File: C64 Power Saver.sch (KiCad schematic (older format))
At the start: 15 parts, among them J1 INPUT, J2 OUTPUT, K1 SANYOU_SRD_Form_C, Q1 PN2222A, Q2 PN2222A

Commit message: Added screw terminals for 9VAC
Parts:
- added J3: 9VAC_INPUT, symbol Screw_Terminal_01x02
- added J4: 9VAC_OUTPUT, symbol Screw_Terminal_01x02
- J1: value INPUT -> 5V_INPUT
- J2: value OUTPUT -> 5V_OUTPUT; symbol POWER -> OUTPUT
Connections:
- wire segments 36 -> 38
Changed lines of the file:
@@
 P 10400 825
 F 0 "J1" H 10400 925 50  0000 C CNN
-F 1 "INPUT" H 10400 625 50  0000 C CNN
+F 1 "5V_INPUT" H 10400 625 50  0000 C CNN
 F 2 "" H 10400 825 50  0001 C CNN
 F 3 "" H 10400 825 50  0001 C CNN
@@
 $EndComp
 $Comp
-L POWER J2
+L OUTPUT J2
 U 1 1 5B8BE0D9
 P 10400 1400
 F 0 "J2" H 10400 1500 50  0000 C CNN
-F 1 "OUTPUT" H 10400 1200 50  0000 C CNN
+F 1 "5V_OUTPUT" H 10400 1200 50  0000 C CNN
 F 2 "" H 10400 1400 50  0001 C CNN
 F 3 "" H 10400 1400 50  0001 C CNN
@@
 	9925 925  9925 1625
 Connection ~ 9925 1500
+$Comp
+L Screw_Terminal_01x02 J3
+U 1 1 5B8C3D4A
+P 8250 925
+F 0 "J3" H 8250 1025 50  0000 C CNN
+F 1 "9VAC_INPUT" H 8250 725 50  0000 C CNN
+F 2 "" H 8250 925 50  0001 C CNN
+F 3 "" H 8250 925 50  0001 C CNN
+	1    8250 925
+	-1   0    0    1
+$EndComp
+$Comp
+L Screw_Terminal_01x02 J4
+U 1 1 5B8C3DC4
+P 9125 825
+F 0 "J4" H 9125 925 50  0000 C CNN
+F 1 "9VAC_OUTPUT" H 9125 625 50  0000 C CNN
+F 2 "" H 9125 825 50  0001 C CNN
+F 3 "" H 9125 825 50  0001 C CNN
+	1    9125 825
+	1    0    0    -1
+$EndComp
+Wire Wire Line
+	8925 825  8450 825
+Wire Wire Line
+	8450 925  8925 925
 $EndSCHEMATC

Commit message: PCB layout done
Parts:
- D1, D2: footprint (none) -> Diodes_THT:D_DO-35_SOD27_P10.16mm_Horizontal
- D3: value LED -> OK; footprint (none) -> LEDs:LED_D5.0mm
- D4: value LED -> OV; footprint (none) -> LEDs:LED_D5.0mm
- F1: footprint (none) -> Fuse_Holders_and_Fuses:Fuseholder5x20_horiz_SemiClosed_Casing10x25mm
- J1, J2, J3, J4: footprint (none) -> Connectors_Terminal_Blocks:TerminalBlock_bornier-2_P5.08mm
- R1, R2, R3, R4, R5: footprint (none) -> Resistors_THT:R_Axial_DIN0207_L6.3mm_D2.5mm_P10.16mm_Horizontal
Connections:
- net labels added: 5V_IN, 5V_OUT, 9VAC_1, 9VAC_2
- net labels removed: VDD
- wire segments 38 -> 40
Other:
- moved on the sheet: J2, J4
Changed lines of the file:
@@
 F 0 "R1" V 2480 2075 50  0000 C CNN
 F 1 "470" V 2400 2075 50  0000 C CNN
-F 2 "" V 2330 2075 50  0001 C CNN
+F 2 "Resistors_THT:R_Axial_DIN0207_L6.3mm_D2.5mm_P10.16mm_Horizontal" V 2330 2075 50  0001 C CNN
 F 3 "" H 2400 2075 50  0001 C CNN
 	1    2400 2075
@@
 F 0 "R2" V 2480 3400 50  0000 C CNN
 F 1 "470" V 2400 3400 50  0000 C CNN
-F 2 "" V 2330 3400 50  0001 C CNN
+F 2 "Resistors_THT:R_Axial_DIN0207_L6.3mm_D2.5mm_P10.16mm_Horizontal" V 2330 3400 50  0001 C CNN
 F 3 "" H 2400 3400 50  0001 C CNN
 	1    2400 3400
@@
 F 0 "R3" V 2955 2075 50  0000 C CNN
 F 1 "2k2" V 2875 2075 50  0000 C CNN
-F 2 "" V 2805 2075 50  0001 C CNN
+F 2 "Resistors_THT:R_Axial_DIN0207_L6.3mm_D2.5mm_P10.16mm_Horizontal" V 2805 2075 50  0001 C CNN
 F 3 "" H 2875 2075 50  0001 C CNN
 	1    2875 2075
@@
 F 0 "D1" H 2400 2750 50  0000 C CNN
 F 1 "4.7v" H 2400 2550 50  0000 C CNN
-F 2 "" H 2400 2650 50  0001 C CNN
+F 2 "Diodes_THT:D_DO-35_SOD27_P10.16mm_Horizontal" H 2400 2650 50  0001 C CNN
 F 3 "" H 2400 2650 50  0001 C CNN
 	1    2400 2650
@@
 F 0 "D2" H 3425 2175 50  0000 C CNN
 F 1 "1N914" H 3425 1975 50  0000 C CNN
-F 2 "" H 3425 2075 50  0001 C CNN
+F 2 "Diodes_THT:D_DO-35_SOD27_P10.16mm_Horizontal" H 3425 2075 50  0001 C CNN
 F 3 "" H 3425 2075 50  0001 C CNN
 	1    3425 2075
@@
 F 0 "R5" V 5630 3525 50  0000 C CNN
 F 1 "470" V 5550 3525 50  0000 C CNN
-F 2 "" V 5480 3525 50  0001 C CNN
+F 2 "Resistors_THT:R_Axial_DIN0207_L6.3mm_D2.5mm_P10.16mm_Horizontal" V 5480 3525 50  0001 C CNN
 F 3 "" H 5550 3525 50  0001 C CNN
 	1    5550 3525
@@
 F 0 "R4" V 5280 3525 50  0000 C CNN
 F 1 "470" V 5200 3525 50  0000 C CNN
-F 2 "" V 5130 3525 50  0001 C CNN
+F 2 "Resistors_THT:R_Axial_DIN0207_L6.3mm_D2.5mm_P10.16mm_Horizontal" V 5130 3525 50  0001 C CNN
 F 3 "" H 5200 3525 50  0001 C CNN
 	1    5200 3525
@@
 P 5550 3975
 F 0 "D4" H 5550 4075 50  0000 C CNN
-F 1 "LED" H 5550 3875 50  0000 C CNN
-F 2 "" H 5550 3975 50  0001 C CNN
+F 1 "OV" H 5550 3875 50  0000 C CNN
+F 2 "LEDs:LED_D5.0mm" H 5550 3975 50  0001 C CNN
 F 3 "" H 5550 3975 50  0001 C CNN
 	1    5550 3975
@@
 P 5200 3975
 F 0 "D3" H 5200 4075 50  0000 C CNN
-F 1 "LED" H 5200 3875 50  0000 C CNN
-F 2 "" H 5200 3975 50  0001 C CNN
+F 1 "OK" H 5200 3875 50  0000 C CNN
+F 2 "LEDs:LED_D5.0mm" H 5200 3975 50  0001 C CNN
 F 3 "" H 5200 3975 50  0001 C CNN
 	1    5200 3975
@@
 F 0 "F1" V 1980 1800 50  0000 C CNN
 F 1 "1.5A" V 1825 1800 50  0000 C CNN
-F 2 "" V 1830 1800 50  0001 C CNN
+F 2 "Fuse_Holders_and_Fuses:Fuseholder5x20_horiz_SemiClosed_Casing10x25mm" V 1830 1800 50  0001 C CNN
 F 3 "" H 1900 1800 50  0001 C CNN
 	1    1900 1800
 	0    1    1    0
 $EndComp
-$Comp
-L VCC #PWR02
-U 1 1 5B8BD26B
-P 1625 1675
-F 0 "#PWR02" H 1625 1525 50  0001 C CNN
-F 1 "VCC" H 1625 1825 50  0000 C CNN
-F 2 "" H 1625 1675 50  0001 C CNN
-F 3 "" H 1625 1675 50  0001 C CNN
-	1    1625 1675
-	1    0    0    -1
-$EndComp
 Wire Wire Line
 	2400 2800 2400 3250
@@
 Connection ~ 5200 2850
 $Comp
-L VCC #PWR03
+L VCC #PWR02
 U 1 1 5B8BE9DD
 P 10075 700
-F 0 "#PWR03" H 10075 550 50  0001 C CNN
+F 0 "#PWR02" H 10075 550 50  0001 C CNN
 F 1 "VCC" H 10075 850 50  0000 C CNN
 F 2 "" H 10075 700 50  0001 C CNN
@@
 $EndComp
 Wire Wire Line
-	10075 1275 10075 1400
-Wire Wire Line
-	10075 1400 10200 1400
-Wire Wire Line
 	10075 700  10075 825
 Wire Wire Line
-	10075 825  10200 825
-$Comp
-L VDD #PWR04
-U 1 1 5B8BF5F3
-P 5200 1675
-F 0 "#PWR04" H 5200 1525 50  0001 C CNN
-F 1 "VDD" H 5200 1825 50  0000 C CNN
-F 2 "" H 5200 1675 50  0001 C CNN
-F 3 "" H 5200 1675 50  0001 C CNN
-	1    5200 1675
-	1    0    0    -1
-$EndComp
-$Comp
-L VDD #PWR05
-U 1 1 5B8BF704
-P 10075 1275
-F 0 "#PWR05" H 10075 1125 50  0001 C CNN
-F 1 "VDD" H 10075 1425 50  0000 C CNN
-F 2 "" H 10075 1275 50  0001 C CNN
-F 3 "" H 10075 1275 50  0001 C CNN
-	1    10075 1275
-	1    0    0    -1
-$EndComp
+	9950 825  10200 825
 $Comp
 L POWER J1
@@
 F 0 "J1" H 10400 925 50  0000 C CNN
 F 1 "5V_INPUT" H 10400 625 50  0000 C CNN
-F 2 "" H 10400 825 50  0001 C CNN
+F 2 "Connectors_Terminal_Blocks:TerminalBlock_bornier-2_P5.08mm" H 10400 825 50  0001 C CNN
 F 3 "" H 10400 825 50  0001 C CNN
 	1    10400 825
@@
 L OUTPUT J2
 U 1 1 5B8BE0D9
-P 10400 1400
-F 0 "J2" H 10400 1500 50  0000 C CNN
-F 1 "5V_OUTPUT" H 10400 1200 50  0000 C CNN
-F 2 "" H 10400 1400 50  0001 C CNN
-F 3 "" H 10400 1400 50  0001 C CNN
-	1    10400 1400
-	1    0    0    -1
-$EndComp
-Wire Wire Line
-	9925 1500 10200 1500
-Wire Wire Line
-	9925 925  10200 925
-$Comp
-L GND #PWR06
+P 10400 1250
+F 0 "J2" H 10400 1350 50  0000 C CNN
+F 1 "5V_OUTPUT" H 10400 1050 50  0000 C CNN
+F 2 "Connectors_Terminal_Blocks:TerminalBlock_bornier-2_P5.08mm" H 10400 1250 50  0001 C CNN
+F 3 "" H 10400 1250 50  0001 C CNN
+	1    10400 1250
+	1    0    0    -1
+$EndComp
+$Comp
+L GND #PWR03
 U 1 1 5B8C250E
-P 9925 1625
-F 0 "#PWR06" H 9925 1375 50  0001 C CNN
-F 1 "GND" H 9925 1475 50  0000 C CNN
-F 2 "" H 9925 1625 50  0001 C CNN
-F 3 "" H 9925 1625 50  0001 C CNN
-	1    9925 1625
-	1    0    0    -1
-$EndComp
-Wire Wire Line
-	9925 925  9925 1625
-Connection ~ 9925 1500
+P 9900 1350
+F 0 "#PWR03" H 9900 1100 50  0001 C CNN
+F 1 "GND" H 9900 1200 50  0000 C CNN
+F 2 "" H 9900 1350 50  0001 C CNN
+F 3 "" H 9900 1350 50  0001 C CNN
+	1    9900 1350
+	1    0    0    -1
+$EndComp
 $Comp
 L Screw_Terminal_01x02 J3
@@
 F 0 "J3" H 8250 1025 50  0000 C CNN
 F 1 "9VAC_INPUT" H 8250 725 50  0000 C CNN
-F 2 "" H 8250 925 50  0001 C CNN
+F 2 "Connectors_Terminal_Blocks:TerminalBlock_bornier-2_P5.08mm" H 8250 925 50  0001 C CNN
 F 3 "" H 8250 925 50  0001 C CNN
 	1    8250 925
@@
 L Screw_Terminal_01x02 J4
 U 1 1 5B8C3DC4
-P 9125 825
-F 0 "J4" H 9125 925 50  0000 C CNN
-F 1 "9VAC_OUTPUT" H 9125 625 50  0000 C CNN
-F 2 "" H 9125 825 50  0001 C CNN
-F 3 "" H 9125 825 50  0001 C CNN
-	1    9125 825
-	1    0    0    -1
-$EndComp
-Wire Wire Line
-	8925 825  8450 825
-Wire Wire Line
-	8450 925  8925 925
+P 8250 1425
+F 0 "J4" H 8250 1525 50  0000 C CNN
+F 1 "9VAC_OUTPUT" H 8250 1225 50  0000 C CNN
+F 2 "Connectors_Terminal_Blocks:TerminalBlock_bornier-2_P5.08mm" H 8250 1425 50  0001 C CNN
+F 3 "" H 8250 1425 50  0001 C CNN
+	1    8250 1425
+	-1   0    0    1
+$EndComp
+Text GLabel 5200 1675 1    60   Output ~ 0
+5V_OUT
+Text GLabel 1625 1675 1    60   Input ~ 0
+5V_IN
+Text GLabel 9950 825  0    60   Output ~ 0
+5V_IN
+Connection ~ 10075 825
+Text GLabel 10075 1475 3    60   Input ~ 0
+5V_OUT
+Wire Wire Line
+	10075 1475 10075 1350
+Wire Wire Line
+	10075 1350 10200 1350
+Wire Wire Line
+	9900 1350 9900 925
+Wire Wire Line
+	9900 925  10200 925
+Wire Wire Line
+	10200 1250 9900 1250
+Connection ~ 9900 1250
+Text GLabel 8575 825  2    60   BiDi ~ 0
+9VAC_1
+Wire Wire Line
+	8450 825  8575 825
+Text GLabel 8575 1425 2    60   BiDi ~ 0
+9VAC_1
+Wire Wire Line
+	8450 1325 8575 1325
+Text GLabel 8575 925  2    60   BiDi ~ 0
+9VAC_2
+Text GLabel 8575 1325 2    60   BiDi ~ 0
+9VAC_2
+Wire Wire Line
+	8450 1425 8575 1425
+Wire Wire Line
+	8450 925  8575 925
 $EndSCHEMATC

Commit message: DIN connector sketch (pads need measuring)
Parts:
- added J5: DIN-7, symbol DIN-7
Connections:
- net 9VAC_1: now also J5.7
- net 9VAC_2: now also J5.6
- net GND: now also J5.2
- net VCC: now also J5.5
- no-connect marks 0 -> 3
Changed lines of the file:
@@
 Wire Wire Line
 	8450 925  8575 925
+$Comp
+L DIN-7 J5
+U 1 1 5B8CBE3E
+P 10075 2650
+F 0 "J5" H 10200 2875 50  0000 C CNN
+F 1 "DIN-7" H 10075 2390 50  0000 C CNN
+F 2 "" H 10075 2650 50  0001 C CNN
+F 3 "" H 10075 2650 50  0001 C CNN
+	1    10075 2650
+	-1   0    0    1
+$EndComp
+$Comp
+L GND #PWR04
+U 1 1 5B8CC381
+P 10075 3075
+F 0 "#PWR04" H 10075 2825 50  0001 C CNN
+F 1 "GND" H 10075 2925 50  0000 C CNN
+F 2 "" H 10075 3075 50  0001 C CNN
+F 3 "" H 10075 3075 50  0001 C CNN
+	1    10075 3075
+	1    0    0    -1
+$EndComp
+Wire Wire Line
+	10075 3075 10075 2950
+NoConn ~ 10375 2650
+NoConn ~ 9775 2650
+NoConn ~ 10375 2750
+Text GLabel 9675 2750 0    60   Output ~ 0
+5V_IN
+Wire Wire Line
+	9675 2750 9775 2750
+Text GLabel 9675 2550 0    60   BiDi ~ 0
+9VAC_1
+Text GLabel 10500 2550 2    60   BiDi ~ 0
+9VAC_2
+Wire Wire Line
+	9675 2550 9775 2550
+Wire Wire Line
+	10375 2550 10500 2550
 $EndSCHEMATC

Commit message: Oh... So I made a saver that works only on bad ones... Rev. B!
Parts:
- D1: value 4.7v -> 1N4732A
- D2: value 1N914 -> 1N4148
- D4: value OV -> BAD
- Q1, Q2: footprint TO_SOT_Packages_THT:TO-92_Molded_Narrow -> TO_SOT_Packages_THT:TO-92_Inline_Wide
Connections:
- net 5V_OUT: now also K1.3; no longer K1.4
- net at R5.1: now also K1.4; no longer K1.3
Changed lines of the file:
@@
 P 2400 2650
 F 0 "D1" H 2400 2750 50  0000 C CNN
-F 1 "4.7v" H 2400 2550 50  0000 C CNN
+F 1 "1N4732A" H 2400 2550 50  0000 C CNN
 F 2 "Diodes_THT:D_DO-35_SOD27_P10.16mm_Horizontal" H 2400 2650 50  0001 C CNN
 F 3 "" H 2400 2650 50  0001 C CNN
@@
 F 0 "Q1" H 2975 3100 50  0000 L CNN
 F 1 "PN2222A" H 2975 3025 50  0000 L CNN
-F 2 "TO_SOT_Packages_THT:TO-92_Molded_Narrow" H 2975 2950 50  0001 L CIN
+F 2 "TO_SOT_Packages_THT:TO-92_Inline_Wide" H 2975 2950 50  0001 L CIN
 F 3 "" H 2775 3025 50  0001 L CNN
 	1    2775 3025
@@
 P 3425 2075
 F 0 "D2" H 3425 2175 50  0000 C CNN
-F 1 "1N914" H 3425 1975 50  0000 C CNN
+F 1 "1N4148" H 3425 1975 50  0000 C CNN
 F 2 "Diodes_THT:D_DO-35_SOD27_P10.16mm_Horizontal" H 3425 2075 50  0001 C CNN
 F 3 "" H 3425 2075 50  0001 C CNN
@@
 F 0 "Q2" H 3525 2725 50  0000 L CNN
 F 1 "PN2222A" H 3525 2650 50  0000 L CNN
-F 2 "TO_SOT_Packages_THT:TO-92_Molded_Narrow" H 3525 2575 50  0001 L CIN
+F 2 "TO_SOT_Packages_THT:TO-92_Inline_Wide" H 3525 2575 50  0001 L CIN
 F 3 "" H 3325 2650 50  0001 L CNN
 	1    3325 2650
@@
 P 5550 3975
 F 0 "D4" H 5550 4075 50  0000 C CNN
-F 1 "OV" H 5550 3875 50  0000 C CNN
+F 1 "BAD" H 5550 3875 50  0000 C CNN
 F 2 "LEDs:LED_D5.0mm" H 5550 3975 50  0001 C CNN
 F 3 "" H 5550 3975 50  0001 C CNN
@@
 	5550 4275 5550 4125
 Wire Wire Line
-	4750 2850 5200 2850
-Wire Wire Line
 	5200 1675 5200 3375
-Wire Wire Line
-	5550 2650 5550 3375
 Connection ~ 2400 1800
 Wire Wire Line
@@
 	5200 4125 5200 4275
 Connection ~ 5200 4275
-Wire Wire Line
-	4750 2650 5550 2650
-Connection ~ 5200 2850
 $Comp
 L VCC #PWR02
@@
 	10075 1350 10200 1350
 Wire Wire Line
-	9900 1350 9900 925
+	9900 925  9900 1350
 Wire Wire Line
 	9900 925  10200 925
@@
 Wire Wire Line
 	10375 2550 10500 2550
+Wire Wire Line
+	4750 2650 5200 2650
+Connection ~ 5200 2650
+Wire Wire Line
+	4750 2850 5550 2850
+Wire Wire Line
+	5550 2850 5550 3375
 $EndSCHEMATC

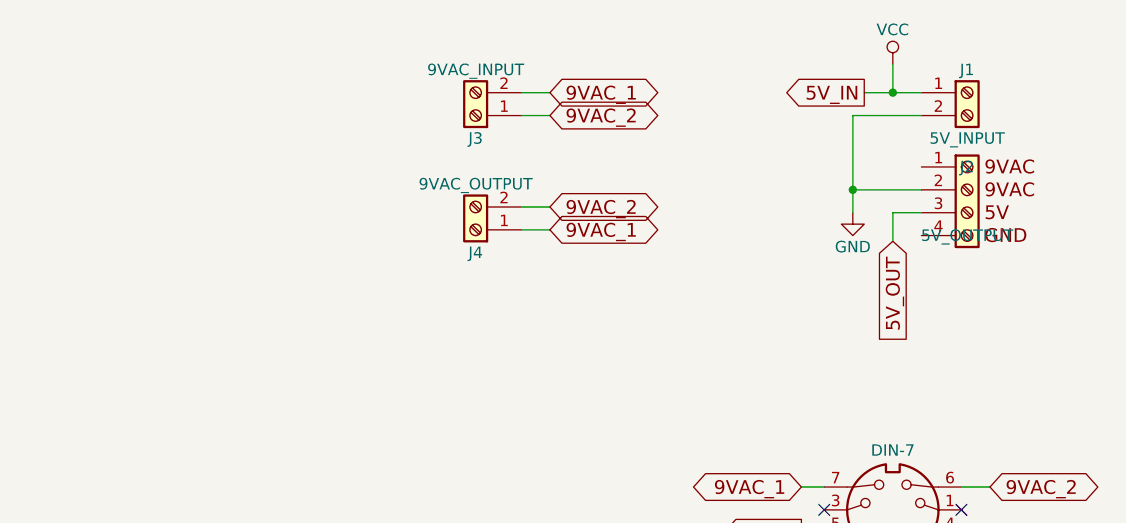
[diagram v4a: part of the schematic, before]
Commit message: Updated schematic to use DIN connector and wire points
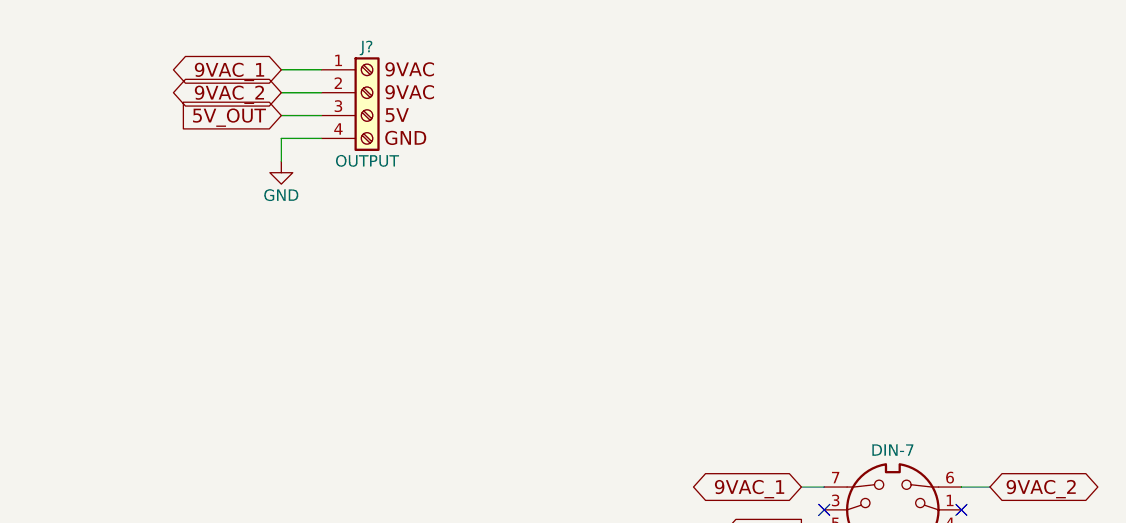
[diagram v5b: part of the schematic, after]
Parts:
- removed J1: 5V_INPUT, Connectors_Terminal_Blocks:TerminalBlock_bornier-2_P5.08mm, symbol POWER
- removed J2: 5V_OUTPUT, Connectors_Terminal_Blocks:TerminalBlock_bornier-2_P5.08mm, symbol OUTPUT
- removed J3: 9VAC_INPUT, Connectors_Terminal_Blocks:TerminalBlock_bornier-2_P5.08mm, symbol Screw_Terminal_01x02
- removed J4: 9VAC_OUTPUT, Connectors_Terminal_Blocks:TerminalBlock_bornier-2_P5.08mm, symbol Screw_Terminal_01x02
- added J?: OUTPUT, symbol OUTPUT
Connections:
- net 5V_OUT: now also J?.3 (Pin_3)
- net 9VAC_1: now also J?.1 (Pin_1)
- net 9VAC_2: now also J?.2 (Pin_2)
- net GND: now also J?.4 (Pin_4)
- net VCC renamed 5V_IN
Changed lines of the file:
@@
 	5200 4125 5200 4275
 Connection ~ 5200 4275
-$Comp
-L VCC #PWR02
-U 1 1 5B8BE9DD
-P 10075 700
-F 0 "#PWR02" H 10075 550 50  0001 C CNN
-F 1 "VCC" H 10075 850 50  0000 C CNN
-F 2 "" H 10075 700 50  0001 C CNN
-F 3 "" H 10075 700 50  0001 C CNN
-	1    10075 700
-	1    0    0    -1
-$EndComp
-Wire Wire Line
-	10075 700  10075 825
-Wire Wire Line
-	9950 825  10200 825
-$Comp
-L POWER J1
-U 1 1 5B8BFF1C
-P 10400 825
-F 0 "J1" H 10400 925 50  0000 C CNN
-F 1 "5V_INPUT" H 10400 625 50  0000 C CNN
-F 2 "Connectors_Terminal_Blocks:TerminalBlock_bornier-2_P5.08mm" H 10400 825 50  0001 C CNN
-F 3 "" H 10400 825 50  0001 C CNN
-	1    10400 825
-	1    0    0    -1
-$EndComp
-$Comp
-L OUTPUT J2
-U 1 1 5B8BE0D9
-P 10400 1250
-F 0 "J2" H 10400 1350 50  0000 C CNN
-F 1 "5V_OUTPUT" H 10400 1050 50  0000 C CNN
-F 2 "Connectors_Terminal_Blocks:TerminalBlock_bornier-2_P5.08mm" H 10400 1250 50  0001 C CNN
-F 3 "" H 10400 1250 50  0001 C CNN
-	1    10400 1250
-	1    0    0    -1
-$EndComp
-$Comp
-L GND #PWR03
-U 1 1 5B8C250E
-P 9900 1350
-F 0 "#PWR03" H 9900 1100 50  0001 C CNN
-F 1 "GND" H 9900 1200 50  0000 C CNN
-F 2 "" H 9900 1350 50  0001 C CNN
-F 3 "" H 9900 1350 50  0001 C CNN
-	1    9900 1350
-	1    0    0    -1
-$EndComp
-$Comp
-L Screw_Terminal_01x02 J3
-U 1 1 5B8C3D4A
-P 8250 925
-F 0 "J3" H 8250 1025 50  0000 C CNN
-F 1 "9VAC_INPUT" H 8250 725 50  0000 C CNN
-F 2 "Connectors_Terminal_Blocks:TerminalBlock_bornier-2_P5.08mm" H 8250 925 50  0001 C CNN
-F 3 "" H 8250 925 50  0001 C CNN
-	1    8250 925
-	-1   0    0    1
-$EndComp
-$Comp
-L Screw_Terminal_01x02 J4
-U 1 1 5B8C3DC4
-P 8250 1425
-F 0 "J4" H 8250 1525 50  0000 C CNN
-F 1 "9VAC_OUTPUT" H 8250 1225 50  0000 C CNN
-F 2 "Connectors_Terminal_Blocks:TerminalBlock_bornier-2_P5.08mm" H 8250 1425 50  0001 C CNN
-F 3 "" H 8250 1425 50  0001 C CNN
-	1    8250 1425
-	-1   0    0    1
-$EndComp
 Text GLabel 5200 1675 1    60   Output ~ 0
 5V_OUT
 Text GLabel 1625 1675 1    60   Input ~ 0
 5V_IN
-Text GLabel 9950 825  0    60   Output ~ 0
-5V_IN
-Connection ~ 10075 825
-Text GLabel 10075 1475 3    60   Input ~ 0
-5V_OUT
-Wire Wire Line
-	10075 1475 10075 1350
-Wire Wire Line
-	10075 1350 10200 1350
-Wire Wire Line
-	9900 925  9900 1350
-Wire Wire Line
-	9900 925  10200 925
-Wire Wire Line
-	10200 1250 9900 1250
-Connection ~ 9900 1250
-Text GLabel 8575 825  2    60   BiDi ~ 0
+Text GLabel 7400 725  0    60   BiDi ~ 0
 9VAC_1
-Wire Wire Line
-	8450 825  8575 825
-Text GLabel 8575 1425 2    60   BiDi ~ 0
-9VAC_1
-Wire Wire Line
-	8450 1325 8575 1325
-Text GLabel 8575 925  2    60   BiDi ~ 0
+Text GLabel 7400 825  0    60   BiDi ~ 0
 9VAC_2
-Text GLabel 8575 1325 2    60   BiDi ~ 0
-9VAC_2
-Wire Wire Line
-	8450 1425 8575 1425
-Wire Wire Line
-	8450 925  8575 925
 $Comp
 L DIN-7 J5
@@
 $EndComp
 $Comp
-L GND #PWR04
+L GND #PWR02
 U 1 1 5B8CC381
 P 10075 3075
-F 0 "#PWR04" H 10075 2825 50  0001 C CNN
+F 0 "#PWR02" H 10075 2825 50  0001 C CNN
 F 1 "GND" H 10075 2925 50  0000 C CNN
 F 2 "" H 10075 3075 50  0001 C CNN
@@
 Wire Wire Line
 	5550 2850 5550 3375
+Wire Wire Line
+	7400 725  7575 725
+Wire Wire Line
+	7400 825  7575 825
+Text GLabel 7400 925  0    60   Input ~ 0
+5V_OUT
+$Comp
+L GND #PWR03
+U 1 1 5BB0E370
+P 7400 1125
+F 0 "#PWR03" H 7400 875 50  0001 C CNN
+F 1 "GND" H 7400 975 50  0000 C CNN
+F 2 "" H 7400 1125 50  0001 C CNN
+F 3 "" H 7400 1125 50  0001 C CNN
+	1    7400 1125
+	1    0    0    -1
+$EndComp
+Wire Wire Line
+	7400 925  7575 925
+Wire Wire Line
+	7575 1025 7400 1025
+Wire Wire Line
+	7400 1025 7400 1125
+$Comp
+L OUTPUT J?
+U 1 1 5BB0E936
+P 7775 825
+F 0 "J?" H 7775 1025 50  0000 C CNN
+F 1 "OUTPUT" H 7775 525 50  0000 C CNN
+F 2 "" H 7775 825 50  0001 C CNN
+F 3 "" H 7775 825 50  0001 C CNN
+	1    7775 825
+	1    0    0    -1
+$EndComp
 $EndSCHEMATC

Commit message: PCB layout redone with DIN connector and added 5v buzzer
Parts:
- added BZ1: Buzzer, Buzzers_Beepers:Buzzer_12x9.5RM7.6, symbol Buzzer
- D1: footprint Diodes_THT:D_DO-35_SOD27_P10.16mm_Horizontal -> Diodes_THT:D_T-1_P10.16mm_Horizontal
- J1: renamed from J?; footprint (none) -> C64_PWR:OUTPUT_ZIP
- J5: footprint (none) -> C64_PWR:C64_PWR
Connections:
- net 9VAC_1: now also J1.2 (Pin_2); no longer J1.1 (Pin_1)
- net 9VAC_2: now also J1.1 (Pin_1); no longer J1.2 (Pin_2)
- net GND: now also BZ1.2 (+)
- net at K1.4, R5.1: now also BZ1.1 (-)
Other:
- moved on the sheet: J1
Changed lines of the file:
@@
 F 0 "D1" H 2400 2750 50  0000 C CNN
 F 1 "1N4732A" H 2400 2550 50  0000 C CNN
-F 2 "Diodes_THT:D_DO-35_SOD27_P10.16mm_Horizontal" H 2400 2650 50  0001 C CNN
+F 2 "Diodes_THT:D_T-1_P10.16mm_Horizontal" H 2400 2650 50  0001 C CNN
 F 3 "" H 2400 2650 50  0001 C CNN
 	1    2400 2650
@@
 	2400 3550 2400 4275
 Wire Wire Line
-	2400 4275 5550 4275
+	2400 4275 5800 4275
 Wire Wire Line
 	3425 2850 3425 4425
@@
 Text GLabel 1625 1675 1    60   Input ~ 0
 5V_IN
-Text GLabel 7400 725  0    60   BiDi ~ 0
+Text GLabel 9775 1550 0    60   BiDi ~ 0
 9VAC_1
-Text GLabel 7400 825  0    60   BiDi ~ 0
+Text GLabel 9775 1450 0    60   BiDi ~ 0
 9VAC_2
 $Comp
@@
 F 0 "J5" H 10200 2875 50  0000 C CNN
 F 1 "DIN-7" H 10075 2390 50  0000 C CNN
-F 2 "" H 10075 2650 50  0001 C CNN
+F 2 "C64_PWR:C64_PWR" H 10075 2650 50  0001 C CNN
 F 3 "" H 10075 2650 50  0001 C CNN
 	1    10075 2650
@@
 Connection ~ 5200 2650
 Wire Wire Line
-	4750 2850 5550 2850
+	4750 2850 5800 2850
 Wire Wire Line
 	5550 2850 5550 3375
 Wire Wire Line
-	7400 725  7575 725
-Wire Wire Line
-	7400 825  7575 825
-Text GLabel 7400 925  0    60   Input ~ 0
+	9775 1450 9950 1450
+Wire Wire Line
+	9775 1550 9950 1550
+Text GLabel 9775 1650 0    60   Input ~ 0
 5V_OUT
 $Comp
 L GND #PWR03
 U 1 1 5BB0E370
-P 7400 1125
-F 0 "#PWR03" H 7400 875 50  0001 C CNN
-F 1 "GND" H 7400 975 50  0000 C CNN
-F 2 "" H 7400 1125 50  0001 C CNN
-F 3 "" H 7400 1125 50  0001 C CNN
-	1    7400 1125
-	1    0    0    -1
-$EndComp
-Wire Wire Line
-	7400 925  7575 925
-Wire Wire Line
-	7575 1025 7400 1025
-Wire Wire Line
-	7400 1025 7400 1125
-$Comp
-L OUTPUT J?
+P 9775 1850
+F 0 "#PWR03" H 9775 1600 50  0001 C CNN
+F 1 "GND" H 9775 1700 50  0000 C CNN
+F 2 "" H 9775 1850 50  0001 C CNN
+F 3 "" H 9775 1850 50  0001 C CNN
+	1    9775 1850
+	1    0    0    -1
+$EndComp
+Wire Wire Line
+	9775 1650 9950 1650
+Wire Wire Line
+	9950 1750 9775 1750
+Wire Wire Line
+	9775 1750 9775 1850
+$Comp
+L OUTPUT J1
 U 1 1 5BB0E936
-P 7775 825
-F 0 "J?" H 7775 1025 50  0000 C CNN
-F 1 "OUTPUT" H 7775 525 50  0000 C CNN
-F 2 "" H 7775 825 50  0001 C CNN
-F 3 "" H 7775 825 50  0001 C CNN
-	1    7775 825
-	1    0    0    -1
-$EndComp
+P 10150 1550
+F 0 "J1" H 10150 1750 50  0000 C CNN
+F 1 "OUTPUT" H 10150 1250 50  0000 C CNN
+F 2 "C64_PWR:OUTPUT_ZIP" H 10150 1550 50  0001 C CNN
+F 3 "" H 10150 1550 50  0001 C CNN
+	1    10150 1550
+	1    0    0    -1
+$EndComp
+$Comp
+L Buzzer BZ1
+U 1 1 5BB0F527
+P 5900 4000
+F 0 "BZ1" H 6050 4050 50  0000 L CNN
+F 1 "Buzzer" H 6050 3950 50  0000 L CNN
+F 2 "Buzzers_Beepers:Buzzer_12x9.5RM7.6" V 5875 4100 50  0001 C CNN
+F 3 "" V 5875 4100 50  0001 C CNN
+	1    5900 4000
+	1    0    0    -1
+$EndComp
+Wire Wire Line
+	5800 4275 5800 4100
+Connection ~ 5550 4275
+Wire Wire Line
+	5800 2850 5800 3900
+Connection ~ 5550 2850
 $EndSCHEMATC
